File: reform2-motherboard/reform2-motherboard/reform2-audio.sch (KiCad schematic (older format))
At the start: 0 parts

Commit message: WIP reform2: more schematics ground work on USB, PCIe, Display, Audio, Power
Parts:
- added J?: SJ-43516-SMT, SJ-43516-SMT, symbol reform2:SJ-43516-SMT
- added U?: TLV320AIC23BPW, Package_SO:TSSOP-28_4.4x9.7mm_P0.65mm, symbol Audio:TLV320AIC23BPW
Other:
- note added: "TODO: other candidates: SGTL5000, WM8731, PCM3168"
- note added: "TODO: potentially a THT connector (more robust?)"
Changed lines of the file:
@@
 Sheet 9 9
 Title ""
-Date ""
+Date "2019-06-21"
 Rev ""
 Comp ""
@@
 Comment4 ""
 $EndDescr
+$Comp
+L Audio:TLV320AIC23BPW U?
+U 1 1 5DC002F7
+P 5800 3750
+F 0 "U?" H 5800 2661 50  0000 C CNN
+F 1 "TLV320AIC23BPW" H 5800 2570 50  0000 C CNN
+F 2 "Package_SO:TSSOP-28_4.4x9.7mm_P0.65mm" H 5800 3750 50  0001 C CIN
+F 3 "http://www.ti.com/lit/ds/symlink/tlv320aic23b.pdf" H 5800 3750 50  0001 C CNN
+	1    5800 3750
+	1    0    0    -1
+$EndComp
+Text Notes 4750 2000 0    50   ~ 0
+TODO: other candidates: SGTL5000, WM8731, PCM3168
+$Comp
+L reform2:SJ-43516-SMT J?
+U 1 1 5DC02AC6
+P 8550 3300
+F 0 "J?" H 8172 3187 50  0000 R CNN
+F 1 "SJ-43516-SMT" H 8172 3278 50  0000 R CNN
+F 2 "SJ-43516-SMT" H 8550 3300 50  0001 L BNN
+F 3 "" H 8550 3300 50  0001 L BNN
+F 4 "Unavailable" H 8550 3300 50  0001 L BNN "Availability"
+F 5 "CUI" H 8550 3300 50  0001 L BNN "MF"
+F 6 "SJ-43516-SMT" H 8550 3300 50  0001 L BNN "MP"
+F 7 "Conn 3.5MM Audio Jack F 6 POS Solder RA SMD 6 Terminal 1 Port" H 8550 3300 50  0001 L BNN "Description"
+F 8 "None" H 8550 3300 50  0001 L BNN "Package"
+	1    8550 3300
+	-1   0    0    1
+$EndComp
+Text Notes 7800 2000 0    50   ~ 0
+TODO: potentially a THT connector (more robust?)
 $EndSCHEMATC

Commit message: WIP reform2: more power/charger details in schematic, footprint fixes
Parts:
- J7: renamed from J?; footprint SJ-43516-SMT -> footprints:SJ-43516-SMT
- gave numbers to parts that had none: 1
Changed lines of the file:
@@
 $EndDescr
 $Comp
-L Audio:TLV320AIC23BPW U?
+L Audio:TLV320AIC23BPW U17
 U 1 1 5DC002F7
 P 5800 3750
-F 0 "U?" H 5800 2661 50  0000 C CNN
+F 0 "U17" H 5800 2661 50  0000 C CNN
 F 1 "TLV320AIC23BPW" H 5800 2570 50  0000 C CNN
 F 2 "Package_SO:TSSOP-28_4.4x9.7mm_P0.65mm" H 5800 3750 50  0001 C CIN
@@
 TODO: other candidates: SGTL5000, WM8731, PCM3168
 $Comp
-L reform2:SJ-43516-SMT J?
+L reform2:SJ-43516-SMT J7
 U 1 1 5DC02AC6
 P 8550 3300
-F 0 "J?" H 8172 3187 50  0000 R CNN
+F 0 "J7" H 8172 3187 50  0000 R CNN
 F 1 "SJ-43516-SMT" H 8172 3278 50  0000 R CNN
-F 2 "SJ-43516-SMT" H 8550 3300 50  0001 L BNN
+F 2 "footprints:SJ-43516-SMT" H 8550 3300 50  0001 L BNN
 F 3 "" H 8550 3300 50  0001 L BNN
 F 4 "Unavailable" H 8550 3300 50  0001 L BNN "Availability"

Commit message: WIP: reform2 motherboard: audio chip and amp
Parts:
- removed U17: TLV320AIC23BPW, Package_SO:TSSOP-28_4.4x9.7mm_P0.65mm, symbol Audio:TLV320AIC23BPW
- added C? (x6): 10uF, symbol Device:C_Small
- added C? (x6): 0.1uF, symbol Device:C_Small
- added C? (x2): 18pF, symbol Device:C_Small
- added C? (x2): 220uF, symbol Device:CP_Small
- added C?: 1uF, symbol Device:CP_Small
- added C? (x2): 22uF, symbol Device:C_Small
- added C? (x2): 15nF, symbol Device:C_Small
- added C? (x2): 1uF, symbol Device:C_Small
- added J?: Conn_01x04_Male, symbol Connector:Conn_01x04_Male
- added R?: 10k, symbol Device:R_Small
- added R?: 100, symbol Device:R_Small
- added R? (x3): 47k, symbol Device:R_Small
- added R?: 2k, symbol Device:R_Small
- added R?: 680, symbol Device:R_Small
- added R?: 0, symbol Device:R_Small
- added U?: WM8731, Package_SO:SSOP-28_5.3x10.2mm_P0.65mm, symbol reform2:WM8731
- added U?: MAX9715ETE+, Package_DFN_QFN:TQFN-16-1EP_5x5mm_P0.8mm_EP3.1x3.1mm, symbol Amplifier_Audio:MAX9715ETE+
- added Y?: 12.288MHz, symbol Device:Crystal_Small
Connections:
- net labels added: +3V3, +5V, DAC_BCLK, DAC_DIN, DAC_DOUT, DAC_MCLK, DAC_RXFS, DAC_SCL, DAC_SDA, DAC_TXFS, GND
- wire segments 0 -> 125
- no-connect marks 0 -> 1
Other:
- note added: "TODO: choke"
- note added: "TODO: chokes?"
- note added: "TODO: gain & shdn"
- note added: "TODO: line in header"
- note added: "TODO: series Rs?"
- note added: "selects 2-wire"
- note removed: "TODO: other candidates: SGTL5000, WM8731, PCM3168"
- moved on the sheet: J7

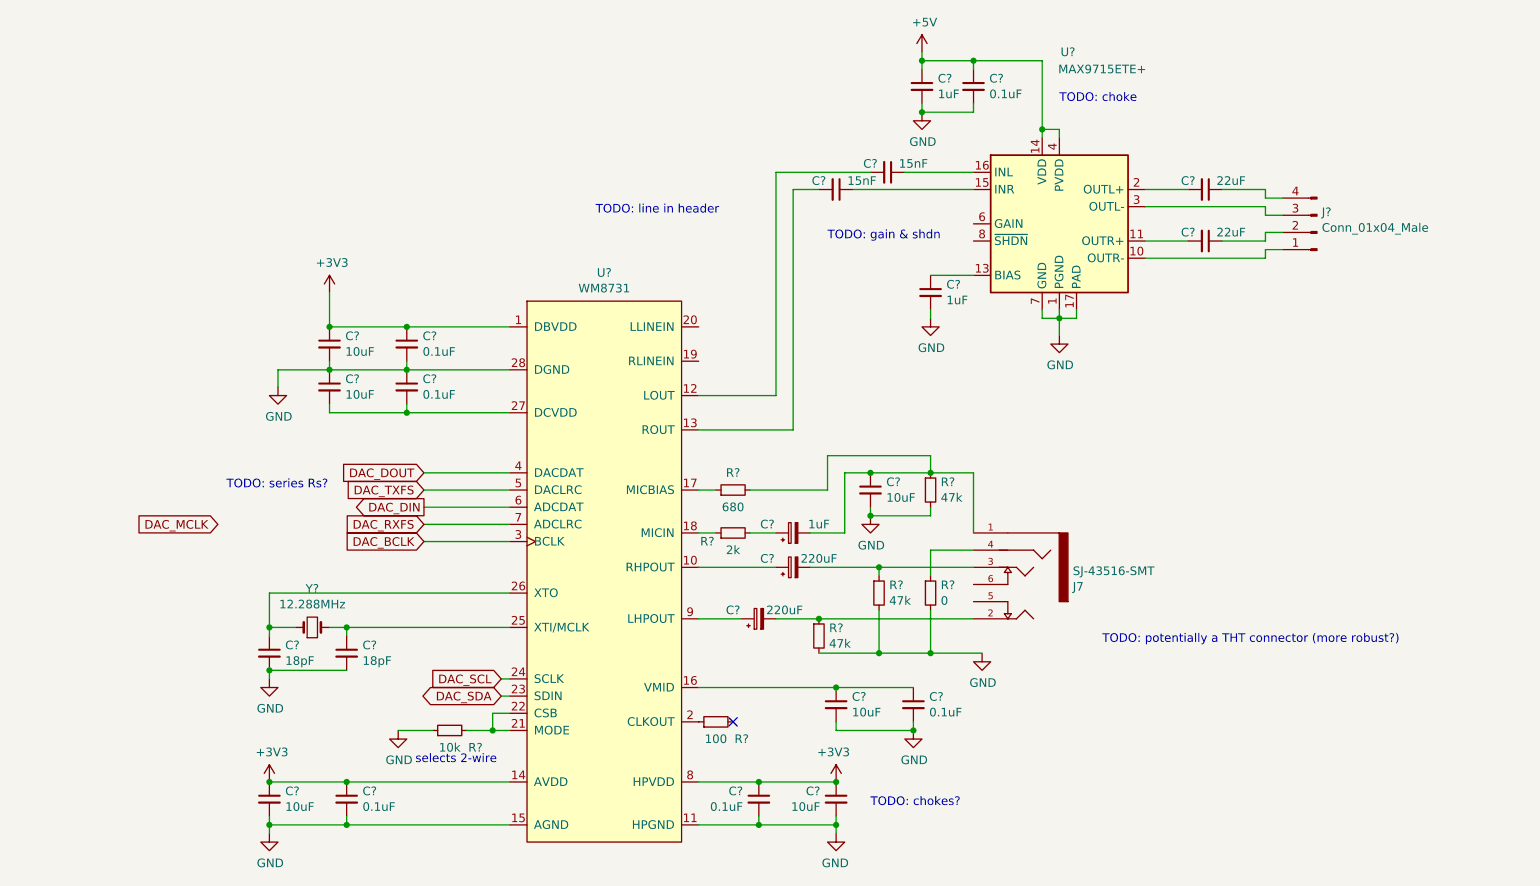
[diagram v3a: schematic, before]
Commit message: WIP: reform2 motherboard: more schematics tuning, preliminary selection of most components
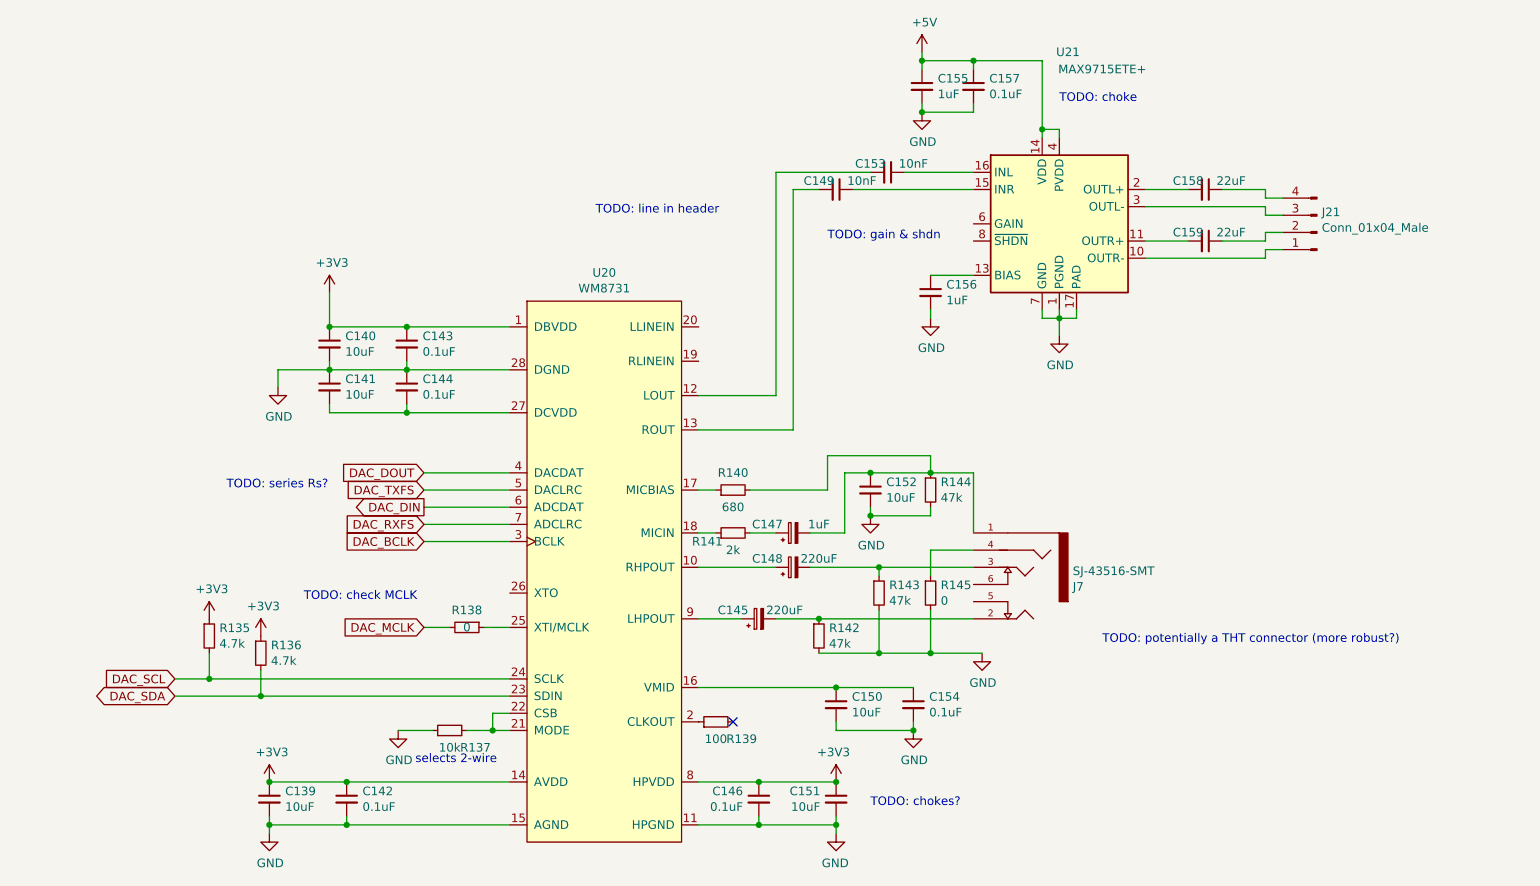
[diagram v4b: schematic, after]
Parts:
- removed C? (x2): 18pF, symbol Device:C_Small
- removed Y?: 12.288MHz, symbol Device:Crystal_Small
- added R135, R136: 4.7k, Resistor_SMD:R_0603_1608Metric, symbol Device:R_Small
- added R138: 0, Resistor_SMD:R_0603_1608Metric, symbol Device:R_Small
- C139, C140, C141, C150, C151, C152: renamed from C?; footprint (none) -> Capacitor_SMD:C_0603_1608Metric; Manufacturer (none) -> Taiyo Yuden; Manufacturer_No (none) -> LMK107BBJ106KALT
- C142, C143, C144, C146, C154, C157: renamed from C?; footprint (none) -> Capacitor_SMD:C_0603_1608Metric; Manufacturer (none) -> TDK; Manufacturer_No (none) -> CGA3E2X8R1E104K080AE
- C145, C148: renamed from C?; footprint (none) -> Capacitor_SMD:CP_Elec_8x10; Manufacturer (none) -> Panasonic; Manufacturer_No (none) -> EEE-FT1H221GP
- C147, C155, C156: renamed from C?; footprint (none) -> Capacitor_SMD:C_0603_1608Metric; Manufacturer (none) -> Taiyo Yuden; Manufacturer_No (none) -> JMK107C6105KA
- C149, C153: renamed from C?; value 15nF -> 10nF; footprint (none) -> Capacitor_SMD:C_0603_1608Metric; Manufacturer (none) -> KEMET; Manufacturer_No (none) -> C0603C103K5RAC3190
- C158, C159: renamed from C?; footprint (none) -> Capacitor_SMD:C_0603_1608Metric; Manufacturer (none) -> KEMET; Manufacturer_No (none) -> EDH226M050S9GAA
- J21: renamed from J?; footprint (none) -> Connector_PinSocket_2.54mm:PinSocket_1x04_P2.54mm_Vertical; Manufacturer (none) -> TE; Manufacturer_No (none) -> 826936-4
- J7: Manufacturer (none) -> CUI; Manufacturer_No (none) -> SJ-43516-SMT
- R137: renamed from R?; footprint (none) -> Resistor_SMD:R_0603_1608Metric; Manufacturer (none) -> Vishay Dale; Manufacturer_No (none) -> CRCW060310K0JNEAC
- R139: renamed from R?; footprint (none) -> Resistor_SMD:R_0603_1608Metric; Manufacturer (none) -> Vishay Dale; Manufacturer_No (none) -> CRCW0603100RFKEAC
- R140, R141: renamed from R?; footprint (none) -> Resistor_SMD:R_0603_1608Metric
- R142, R143, R144: renamed from R?; footprint (none) -> Resistor_SMD:R_0603_1608Metric; Manufacturer (none) -> Vishay Dale; Manufacturer_No (none) -> CRCW060347K0FKEAC
- R145: renamed from R?; footprint (none) -> Resistor_SMD:R_0603_1608Metric; Manufacturer (none) -> Vishay Dale; Manufacturer_No (none) -> CRCW06030000Z0EAC
- U20: renamed from U?; Manufacturer (none) -> Cirrus Logic; Manufacturer_No (none) -> WM8731
- U21: renamed from U?; Manufacturer (none) -> Maxim Integrated; Manufacturer_No (none) -> MAX9715ETE+
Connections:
- net +3V3: now also R135.1, R136.1
- net DAC_MCLK: now also R138.2
- net DAC_SCL: now also R135.2
- net DAC_SDA: now also R136.2
- net at U20.25 (XTI/MCLK): now also R138.1
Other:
- note added: "TODO: check MCLK"

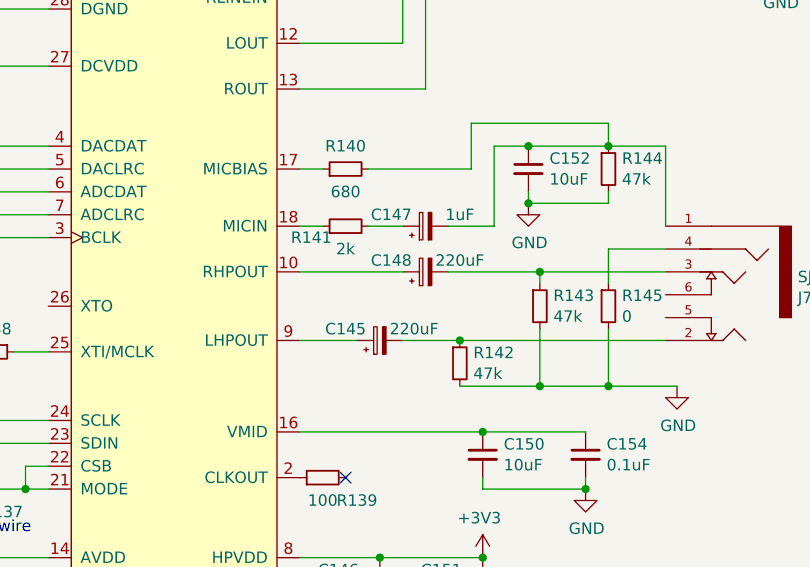
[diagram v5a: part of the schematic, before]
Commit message: WIP: reform 2 motherboard: initial power section placement, routing tests
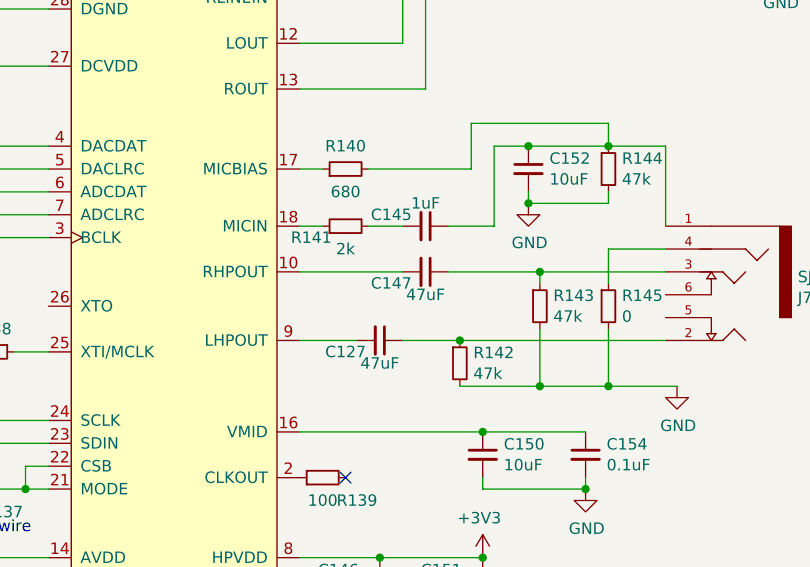
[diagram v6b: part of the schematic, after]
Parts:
- removed C145, C148: 220uF, Capacitor_SMD:CP_Elec_8x10, symbol Device:CP_Small
- removed C147: 1uF, Capacitor_SMD:C_0603_1608Metric, symbol Device:CP_Small
- added C127, C147: 47uF, Capacitor_SMD:C_0603_1608Metric, symbol Device:C_Small
- added C145: 1uF, Capacitor_SMD:C_0603_1608Metric, symbol Device:C_Small
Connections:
- net at C152.1, J7.1 (SLEEVE), R140.2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: now also C145.1
- net at J7.2 (TIP), R142.1: now also C127.1
- net at J7.3 (RING1), R143.1: now also C147.1
- net at U20.10 (RHPOUT): now also C147.2
- net at U20.9 (LHPOUT): now also C127.2
- net at R141.2: now also C145.2
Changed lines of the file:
@@
 Sheet 9 9
 Title "Reform 2 Audio"
-Date "2019-07-09"
-Rev "0.1.1"
+Date "2019-07-10"
+Rev "0.1.2"
 Comp "MNT Research GmbH"
 Comment1 "https://mntre.com"
@@
 	6100 5950 6100 5900
 Connection ~ 6100 5900
-$Comp
-L Device:CP_Small C145
-U 1 1 5F0D443E
-P 5650 4700
-F 0 "C145" V 5700 4850 50  0000 C CNN
-F 1 "220uF" V 5700 4550 50  0000 C CNN
-F 2 "Capacitor_SMD:CP_Elec_8x10" H 5650 4700 50  0001 C CNN
-F 3 "~" H 5650 4700 50  0001 C CNN
-F 4 "Panasonic" H 5650 4700 50  0001 C CNN "Manufacturer"
-F 5 "EEE-FT1H221GP" H 5650 4700 50  0001 C CNN "Manufacturer_No"
-	1    5650 4700
-	0    -1   -1   0
-$EndComp
 Wire Wire Line
 	5550 4700 5300 4700
 Wire Wire Line
 	5750 4700 6000 4700
-$Comp
-L Device:CP_Small C148
-U 1 1 5F0D63B2
-P 5850 4400
-F 0 "C148" V 5900 4550 50  0000 C CNN
-F 1 "220uF" V 5900 4250 50  0000 C CNN
-F 2 "Capacitor_SMD:CP_Elec_8x10" H 5850 4400 50  0001 C CNN
-F 3 "~" H 5850 4400 50  0001 C CNN
-F 4 "Panasonic" H 5850 4400 50  0001 C CNN "Manufacturer"
-F 5 "EEE-FT1H221GP" H 5850 4400 50  0001 C CNN "Manufacturer_No"
-	1    5850 4400
-	0    -1   -1   0
-$EndComp
 Wire Wire Line
 	5950 4400 6350 4400
@@
 Wire Wire Line
 	6350 4900 6000 4900
-$Comp
-L Device:CP_Small C147
-U 1 1 5F0E0306
-P 5850 4200
-F 0 "C147" V 5900 4350 50  0000 C CNN
-F 1 "1uF" V 5900 4050 50  0000 C CNN
-F 2 "Capacitor_SMD:C_0603_1608Metric" H 5850 4200 50  0001 C CNN
-F 3 "~" H 5850 4200 50  0001 C CNN
-F 4 "Taiyo Yuden" H 5850 4200 50  0001 C CNN "Manufacturer"
-F 5 "JMK107C6105KA" H 5850 4200 50  0001 C CNN "Manufacturer_No"
-	1    5850 4200
-	0    -1   -1   0
-$EndComp
 $Comp
 L Device:C_Small C152
@@
 Wire Wire Line
 	2750 5150 4200 5150
+$Comp
+L Device:C_Small C147
+U 1 1 5F2211CD
+P 5850 4400
+F 0 "C147" V 5900 4250 50  0000 C CNN
+F 1 "47uF" V 5950 4400 50  0000 C CNN
+F 2 "Capacitor_SMD:C_0603_1608Metric" H 5850 4400 50  0001 C CNN
+F 3 "~" H 5850 4400 50  0001 C CNN
+	1    5850 4400
+	0    1    1    0
+$EndComp
+$Comp
+L Device:C_Small C127
+U 1 1 5F2217E7
+P 5650 4700
+F 0 "C127" V 5700 4550 50  0000 C CNN
+F 1 "47uF" V 5750 4700 50  0000 C CNN
+F 2 "Capacitor_SMD:C_0603_1608Metric" H 5650 4700 50  0001 C CNN
+F 3 "~" H 5650 4700 50  0001 C CNN
+	1    5650 4700
+	0    1    1    0
+$EndComp
+$Comp
+L Device:C_Small C145
+U 1 1 5F221A6E
+P 5850 4200
+F 0 "C145" V 5800 4050 50  0000 C CNN
+F 1 "1uF" V 5750 4200 50  0000 C CNN
+F 2 "Capacitor_SMD:C_0603_1608Metric" H 5850 4200 50  0001 C CNN
+F 3 "~" H 5850 4200 50  0001 C CNN
+	1    5850 4200
+	0    1    1    0
+$EndComp
 $EndSCHEMATC
